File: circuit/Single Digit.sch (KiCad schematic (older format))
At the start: 40 parts

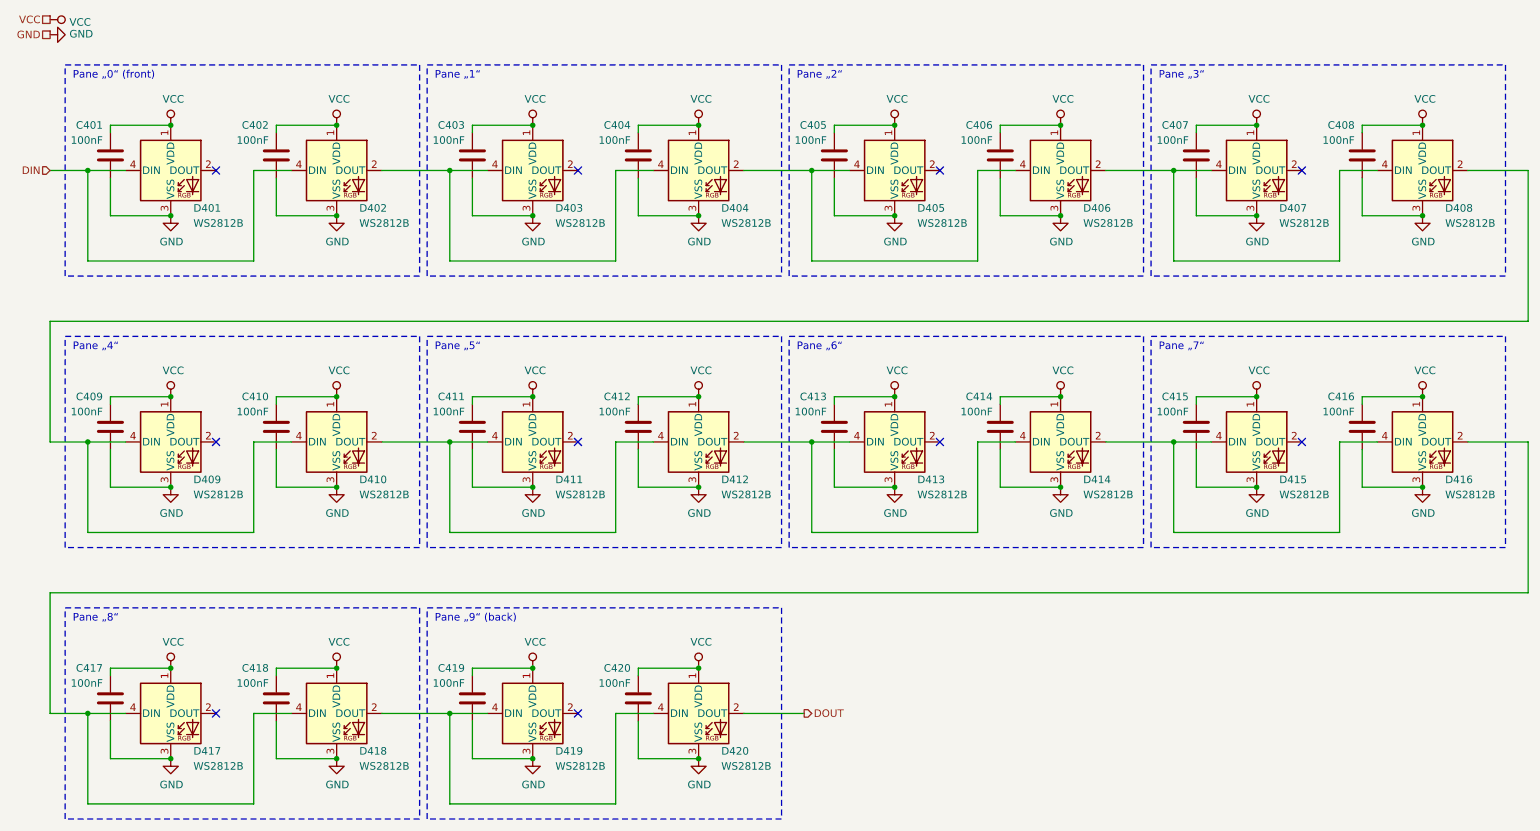
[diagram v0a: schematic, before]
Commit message: Improve schematics, add crystals, USB connector, power regulator, backup battery
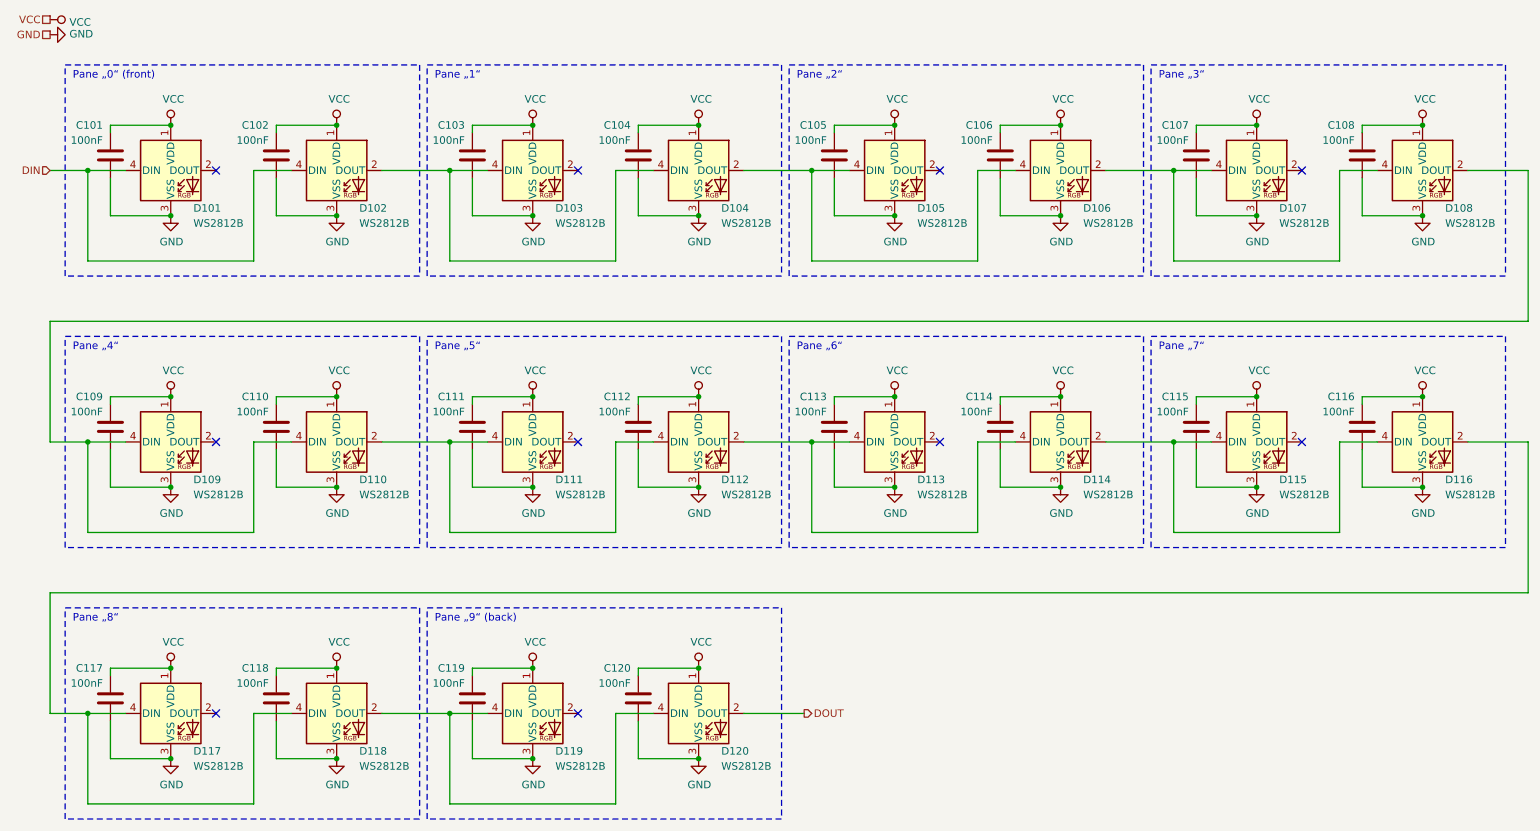
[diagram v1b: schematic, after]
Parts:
- C101, C102, C103, C104, C105, C106, C107, C108, C109, C110, C111, C112, C113, C114, C115, C116, C117, C118, C119, C120: footprint Capacitor_SMD:C_0805_2012Metric -> Capacitor_SMD:C_0805_2012Metric_Pad1.15x1.40mm_HandSolder
